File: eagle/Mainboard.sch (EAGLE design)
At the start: 9 parts, among them IC1 L293D, IC2 TLC272P

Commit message: -
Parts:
- removed JP1, JP2: (no value), pinhead:PINHD-1X17
- added IC3: LM1085IT-5.0, burr-brown:REG1117F
- added R1, R2: (no value), rcl:R-EU_RDH/15
- added SV1, SV2: (no value), con-lsta:FE20-1
- added U$1: SCHALTER-1XUM, bs_lib:SCHALTER-1XUM
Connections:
- new net M: BATT1.M, IC1.GND1, IC1.GND2, IC1.GND3, IC1.GND4, IC3.GND, R1.1, R2.1
- new net N$1: IC1.VCC2, IC3.VIN, U$1.P$2
- new net N$10: R2.2, REFL2.C
- new net N$2: REFL1.A, REFL1.COL, REFL2.A, REFL2.COL
- new net N$3: IC1.1-2EN, IC1.3-4EN, IC1.VCC1, IC3.VOUT
- new net N$4: IC1.1Y, MOT1.P$2
- new net N$5: IC1.2Y, MOT1.P$1
- new net N$6: IC1.4Y, MOT2.P$2
- new net N$7: IC1.3Y, MOT2.P$1
- new net N$9: R1.2, REFL1.C
- new net P: BATT1.P, U$1.P$1
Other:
- note added: "(FCLK)"
- note added: "(FCS)"
- note added: "(FSD0)"
- note added: "(FSD1)"
- note added: "(FSD2)"
- note added: "(FSD3)"
- note added: "EN"
- note added: "EXT_5V"
- note added: "FSVN"
- note added: "FSVP"
- note added: "GND"
- note added: "IO0"
- note added: "IO10"
- note added: "IO12"
- note added: "IO13"
- note added: "IO14"
- note added: "IO15"
- note added: "IO18"
- note added: "IO19"
- note added: "IO2"
- note added: "IO21"
- note added: "IO22"
- note added: "IO23"
- note added: "IO25"
- note added: "IO26"
- note added: "IO27"
- note added: "IO32"
- note added: "IO33"
- note added: "IO34"
- note added: "IO35"
- note added: "IO37"
- note added: "IO38"
- note added: "IO4"
- note added: "IO5"
- note added: "IO9"
- note added: "RXD0"
- note added: "TXD0"
- note added: "VDD33"
- moved on the sheet: BATT1, IC1, IC2A, IC2B, MOT1, MOT2, REFL1, REFL2

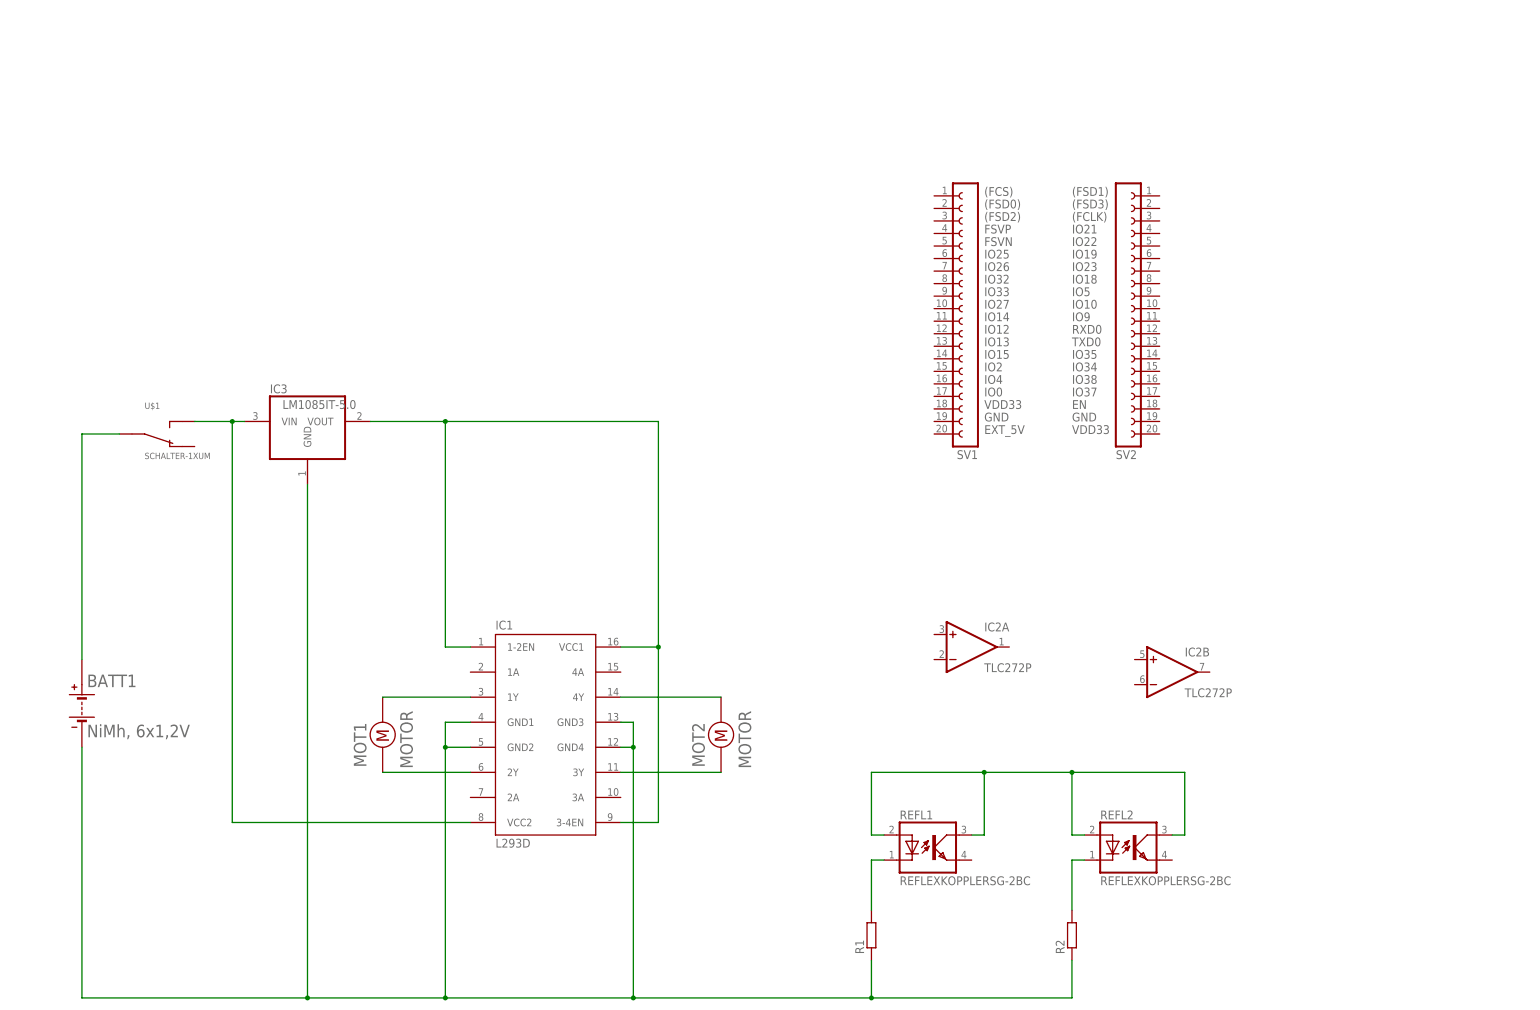
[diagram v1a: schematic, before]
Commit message: erweitert um Ultraschallsensoren
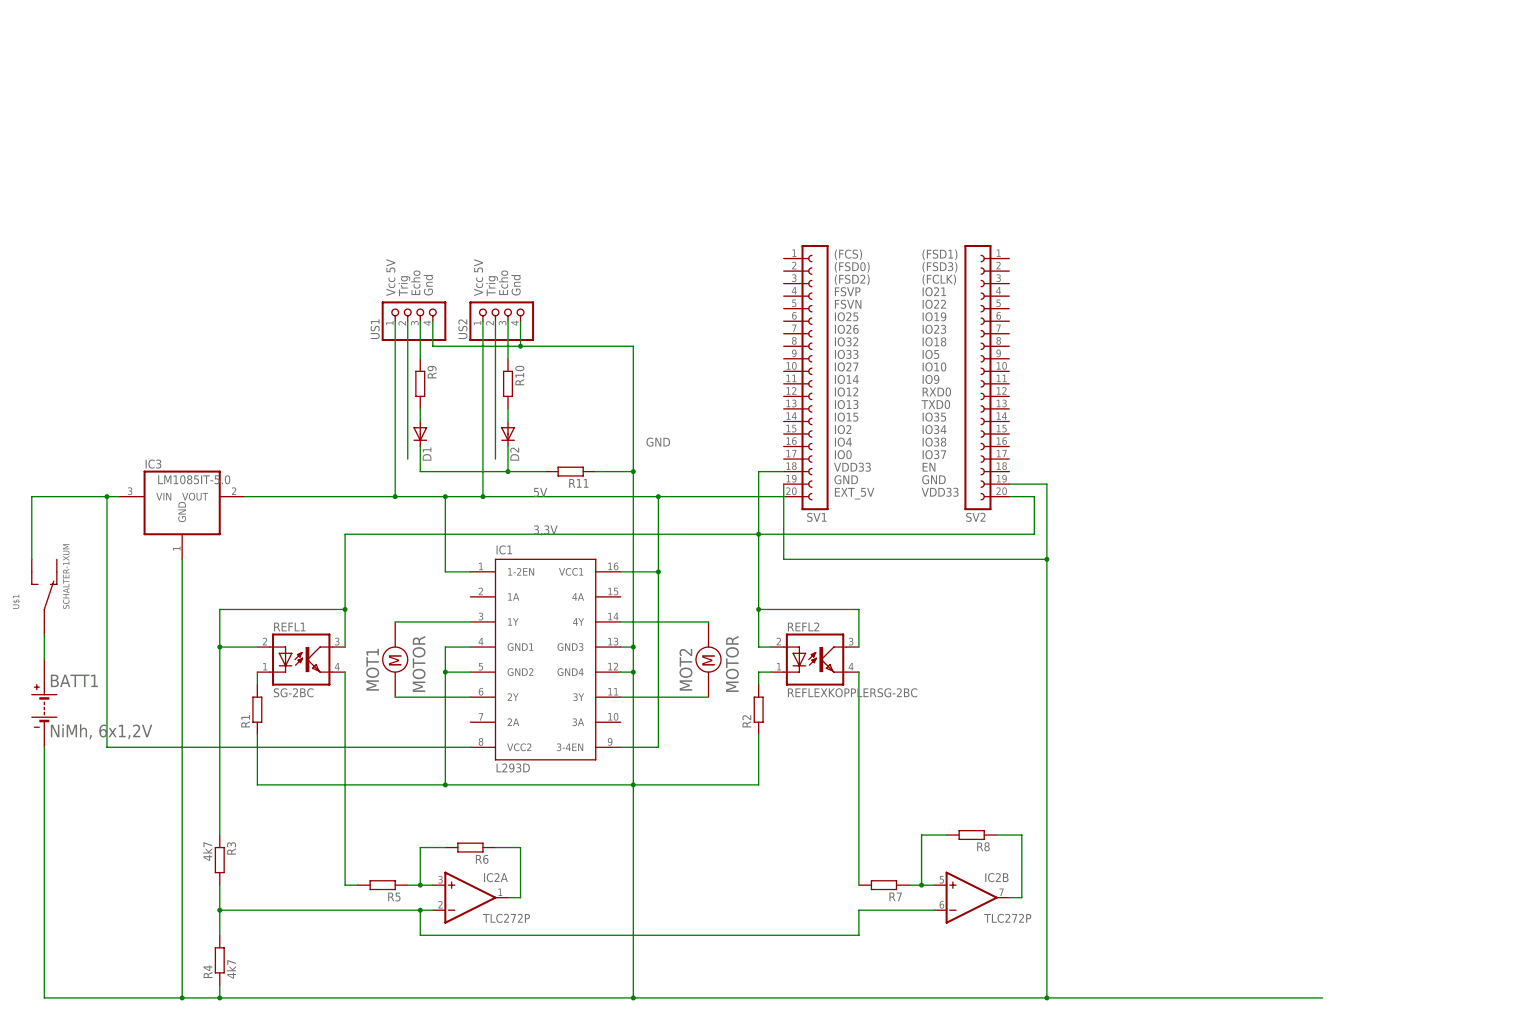
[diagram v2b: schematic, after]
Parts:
- added D1, D2: 1N4148DO35-10, diode:1N4148DO35-10
- added R10, R11, R5, R6, R7, R8, R9: (no value), rcl:R-EU_RDH/15
- added R3, R4: 4k7, rcl:R-EU_RDH/15
- added US1, US2: (no value), pinhead:PINHD-1X4
- REFL1: value REFLEXKOPPLERSG-2BC -> SG-2BC
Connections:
- removed net M: BATT1.M, IC1.GND1, IC1.GND2, IC1.GND3, IC1.GND4, IC3.GND, R1.1, R2.1
- new net 3,3V: R3.1, REFL1.A, REFL1.COL, REFL2.A, REFL2.COL, SV1.18, SV2.20
- new net 5V: IC1.1-2EN, IC1.3-4EN, IC1.VCC1, IC3.VOUT, SV1.20, US1.1, US2.1
- new net GND: BATT1.M, IC1.GND1, IC1.GND2, IC1.GND3, IC1.GND4, IC3.GND, R1.1, R11.1, R2.1, R4.1, SV1.19, SV2.19, US1.4, US2.4
- new net N$1: D1.A, R9.2
- new net N$12: US1.2
- new net N$13: US2.2
- new net N$14: R9.1, US1.3
- new net N$15: R10.1, US2.3
- new net N$19: R5.2, REFL1.EMIT
- new net N$21: IC2A.OUT, R6.1
- new net N$22: IC2A.+IN, R5.1, R6.2
- new net N$23: IC2A.-IN, IC2B.-IN, R3.2, R4.2
- new net N$24: IC2B.+IN, R7.1, R8.2
- new net N$25: IC2B.OUT, R8.1
- new net N$26: R7.2, REFL2.EMIT
- net N$2: now also D2.A, R10.2; no longer REFL1.A, REFL1.COL, REFL2.A, REFL2.COL
- net N$3: now also D1.C, D2.C, R11.2; no longer IC1.1-2EN, IC1.3-4EN, IC1.VCC1, IC3.VOUT
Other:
- note added: "Echo"
- note added: "Gnd"
- note added: "Trig"
- note added: "Vcc 5V"
- moved on the sheet: BATT1, IC1, IC2A, IC2B, IC3, MOT1, MOT2, R1, R2, REFL1, REFL2, SV1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

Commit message: Display hinzugefügt
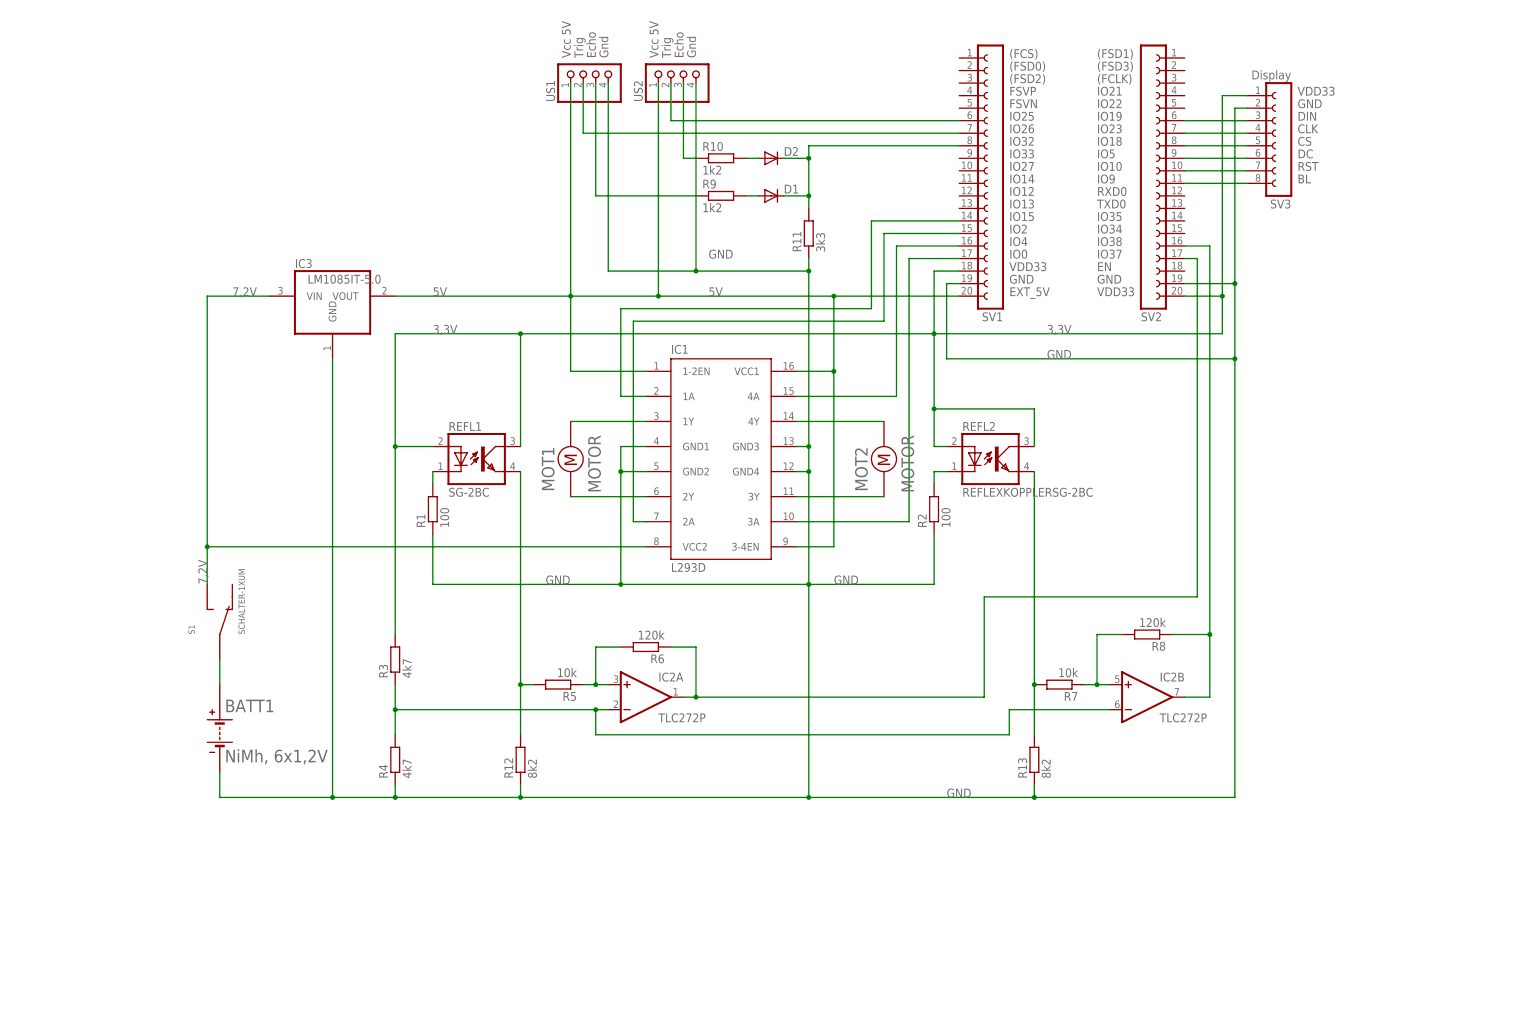
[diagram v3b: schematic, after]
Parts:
- removed U$1: SCHALTER-1XUM, bs_lib:SCHALTER-1XUM
- added R12, R13: 8k2, rcl:R-EU_RDH/15
- added S1: SCHALTER-1XUM, bs_lib:SCHALTER-1XUM
- added SV3: Display, con-lsta:FE08-1
- R1, R2: value (none) -> 100
- R10, R9: value (none) -> 1k2
- R11: value (none) -> 3k3
- R5, R7: value (none) -> 10k
- R6, R8: value (none) -> 120k
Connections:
- removed net N$20: IC1.VCC2, IC3.VIN, U$1.P$2
- removed net N$25: IC2B.OUT, R8.1
- new net 7,2V: IC1.VCC2, IC3.VIN, S1.P$2
- new net N$11: SV2.7, SV3.4
- new net N$16: SV2.8, SV3.5
- new net N$17: SV2.9, SV3.6
- new net N$18: SV2.10, SV3.7
- new net N$27: SV2.11, SV3.8
- new net N$28: IC2B.OUT, R8.1, SV2.16
- new net N$29: IC1.3A, SV1.17
- new net N$30: IC1.4A, SV1.16
- new net N$31: IC1.1A, SV1.14
- new net N$32: IC1.2A, SV1.15
- new net N$8: SV2.6, SV3.3
- net 3,3V: now also R3.2, SV3.1; no longer R3.1
- net GND: now also R12.1, R13.1, SV3.2
- net N$12: now also SV1.7
- net N$13: now also SV1.6
- net N$19: now also R12.2
- net N$21: now also SV2.17
- net N$23: now also R3.1; no longer R3.2
- net N$26: now also R13.2
- net N$3: now also SV1.8
- net P: now also S1.P$1; no longer U$1.P$1
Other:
- note added: "BL"
- note added: "CLK"
- note added: "CS"
- note added: "DC"
- note added: "DIN"
- note added: "RST"
- moved on the sheet: BATT1, D1, D2, IC1, IC2A, IC2B, IC3, MOT1, MOT2, R1, R10, R11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
